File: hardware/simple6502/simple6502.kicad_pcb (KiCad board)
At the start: 2 copper layers, 100 x 100 mm, 40 parts, among them J1 ~{VP}, J2 CLK SEL, J3 RESET, J4 GND, J5 POWER 5V, J6 AUX 5VDC, J7 FTDI Serial, J8 USB Power, J9 Expansion Port, SW1 RESET, SW2 POWER, T1 DS1813, U1 W65C02SxP, U2 RAM 62256, U3 ROM 28C256, U4 74LS30, U5 74HCT00, U6 74HC138, U7 MC68B50, X1 ACO-1MHz

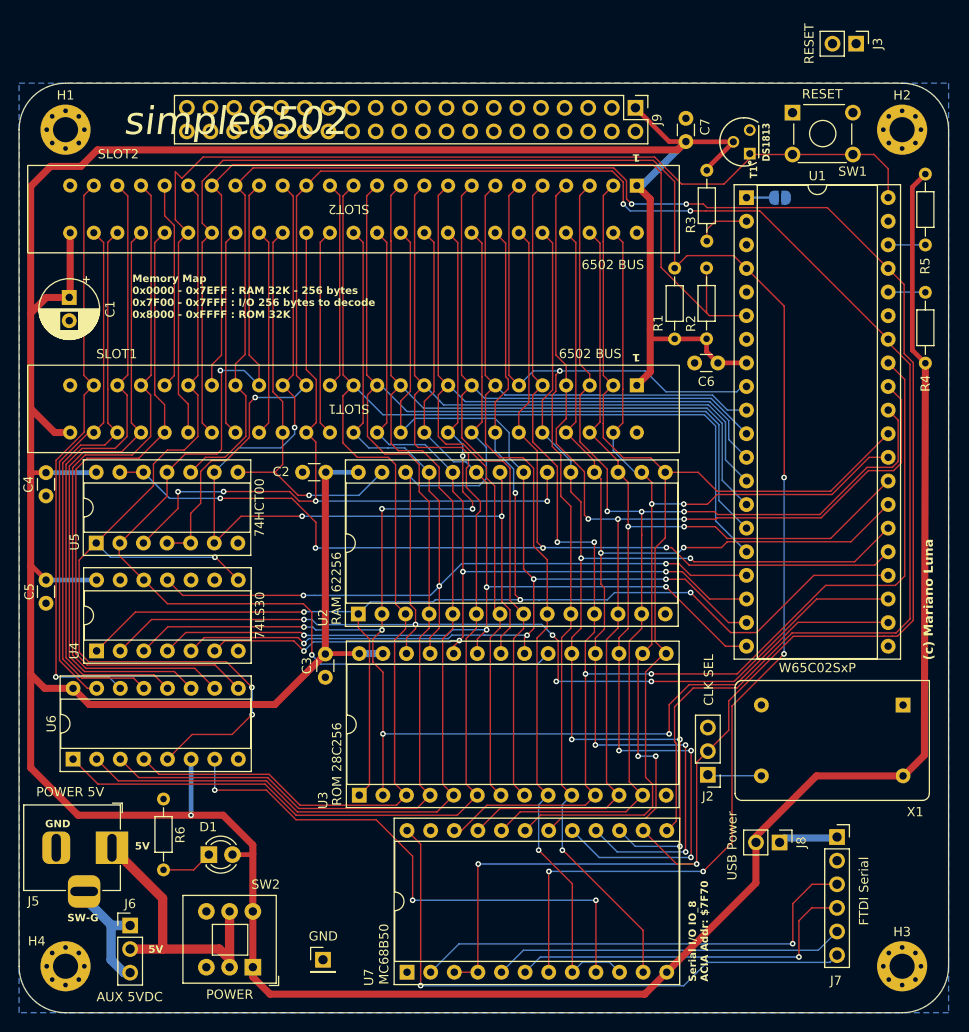
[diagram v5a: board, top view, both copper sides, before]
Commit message: port wired, new slot pinout
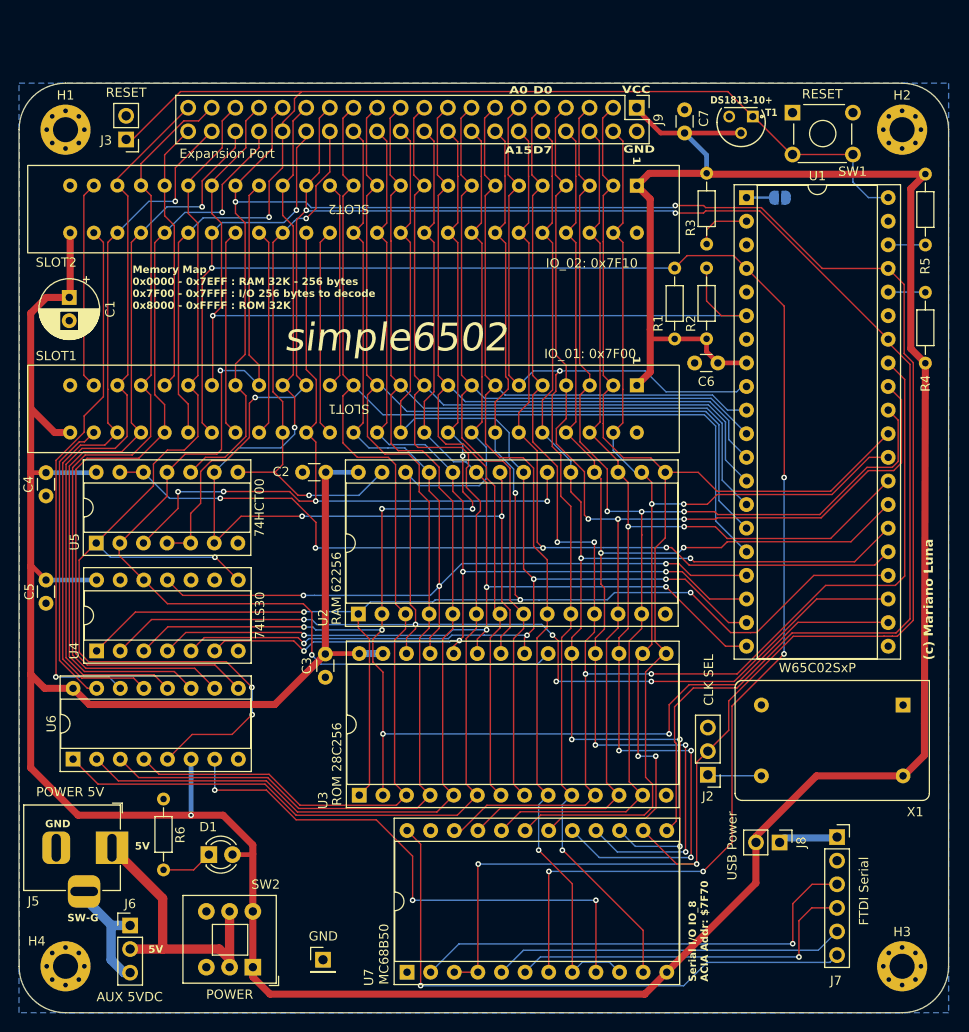
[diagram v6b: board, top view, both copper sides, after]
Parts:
- SLOT1: value 6502 BUS -> IO_01: 0x7F00
- SLOT2: value 6502 BUS -> IO_02: 0x7F10
- T1: value DS1813 -> DS1813-10+
- moved J3 79.2 mm to (61.5, 56.0), turned to 180 degrees
- moved T1 0.96 mm to (126.4, 54.9), turned to 180 degrees
- moved C7 0.93 mm to (121.6, 55.4)
- moved R3 0.32 mm to (124.0, 67.3)
- moved J9 0.14 mm to (116.5, 52.6)
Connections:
- net NC33 renamed BUS_33
- net NC34 renamed BUS_34
- J9 pad 10: unconnected-(J9-Pin_10-Pad10) -> D7
- J9 pad 11: unconnected-(J9-Pin_11-Pad11) -> A0
- J9 pad 12: unconnected-(J9-Pin_12-Pad12) -> A15
- J9 pad 13: unconnected-(J9-Pin_13-Pad13) -> A1
- J9 pad 14: unconnected-(J9-Pin_14-Pad14) -> A14
- J9 pad 15: unconnected-(J9-Pin_15-Pad15) -> A2
- J9 pad 16: unconnected-(J9-Pin_16-Pad16) -> A13
- J9 pad 17: unconnected-(J9-Pin_17-Pad17) -> A3
- J9 pad 18: unconnected-(J9-Pin_18-Pad18) -> A12
- J9 pad 19: unconnected-(J9-Pin_19-Pad19) -> A4
- J9 pad 20: unconnected-(J9-Pin_20-Pad20) -> A11
- J9 pad 21: unconnected-(J9-Pin_21-Pad21) -> A5
- J9 pad 22: unconnected-(J9-Pin_22-Pad22) -> A10
- J9 pad 23: unconnected-(J9-Pin_23-Pad23) -> A6
- J9 pad 24: unconnected-(J9-Pin_24-Pad24) -> A9
- J9 pad 25: unconnected-(J9-Pin_25-Pad25) -> A7
- J9 pad 26: unconnected-(J9-Pin_26-Pad26) -> A8
- J9 pad 27: unconnected-(J9-Pin_27-Pad27) -> R~{W}
- J9 pad 28: unconnected-(J9-Pin_28-Pad28) -> ~{WR}
- J9 pad 29: unconnected-(J9-Pin_29-Pad29) -> ~{RD}
- J9 pad 3: unconnected-(J9-Pin_3-Pad3) -> D3
- J9 pad 30: unconnected-(J9-Pin_30-Pad30) -> ~{IRQ}
- J9 pad 31: unconnected-(J9-Pin_31-Pad31) -> CLK
- J9 pad 32: unconnected-(J9-Pin_32-Pad32) -> ~{RESET}
- J9 pad 33: unconnected-(J9-Pin_33-Pad33) -> ~{NMI}
- J9 pad 34: unconnected-(J9-Pin_34-Pad34) -> ~{IO_07}
- J9 pad 35: unconnected-(J9-Pin_35-Pad35) -> ~{IO_CS}
- J9 pad 36: unconnected-(J9-Pin_36-Pad36) -> ~{IO_05}
- J9 pad 37: unconnected-(J9-Pin_37-Pad37) -> ~{IO_06}
- J9 pad 38: unconnected-(J9-Pin_38-Pad38) -> ~{IO_03}
- J9 pad 39: unconnected-(J9-Pin_39-Pad39) -> ~{IO_04}
- J9 pad 4: unconnected-(J9-Pin_4-Pad4) -> D4
- J9 pad 40: unconnected-(J9-Pin_40-Pad40) -> BUS_21
- J9 pad 5: unconnected-(J9-Pin_5-Pad5) -> D2
- J9 pad 6: unconnected-(J9-Pin_6-Pad6) -> D5
- J9 pad 7: unconnected-(J9-Pin_7-Pad7) -> D1
- J9 pad 8: unconnected-(J9-Pin_8-Pad8) -> D6
- J9 pad 9: unconnected-(J9-Pin_9-Pad9) -> D0
- SLOT1 pad 21: ~{IO_NC} -> BUS_21
- SLOT1 pad 24: ~{IO_02} -> BUS_24
- SLOT2 pad 21: ~{IO_NC} -> BUS_21
- SLOT2 pad 24: ~{IO_02} -> BUS_24
- SLOT2 pad 27: ~{IO_01} -> ~{IO_02}
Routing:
- net VCC: track 491.4 -> 431.5 mm
- net BUS_21: track 0.00 -> 29.2 mm
- net ~{RESET}: track 114.1 -> 137.3 mm, vias 0 -> 1
- net BUS_24: track 0.00 -> 22.4 mm
- net ~{IO_01}: track 54.0 -> 31.6 mm
- net ~{IO_NC}: track 22.4 -> 0.00 mm
- net ~{IO_07}: track 72.4 -> 89.9 mm, vias 0 -> 1
- net ~{IO_05}: track 66.6 -> 83.9 mm, vias 0 -> 1
- net ~{IO_03}: track 60.7 -> 77.5 mm, vias 0 -> 1
- net ~{WR}: track 44.5 -> 58.1 mm, vias 1 -> 2
- net ~{IO_06}: track 75.0 -> 87.5 mm
- net A15: track 125.0 -> 136.8 mm
- net D5: track 123.1 -> 134.8 mm
- net D6: track 123.0 -> 134.8 mm
- net D7: track 122.6 -> 134.4 mm
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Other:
- board text added: "A0"
- board text added: "A15"
- board text added: "D0"
- board text added: "D7"
- board text added: "VCC"

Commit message: minor route changes
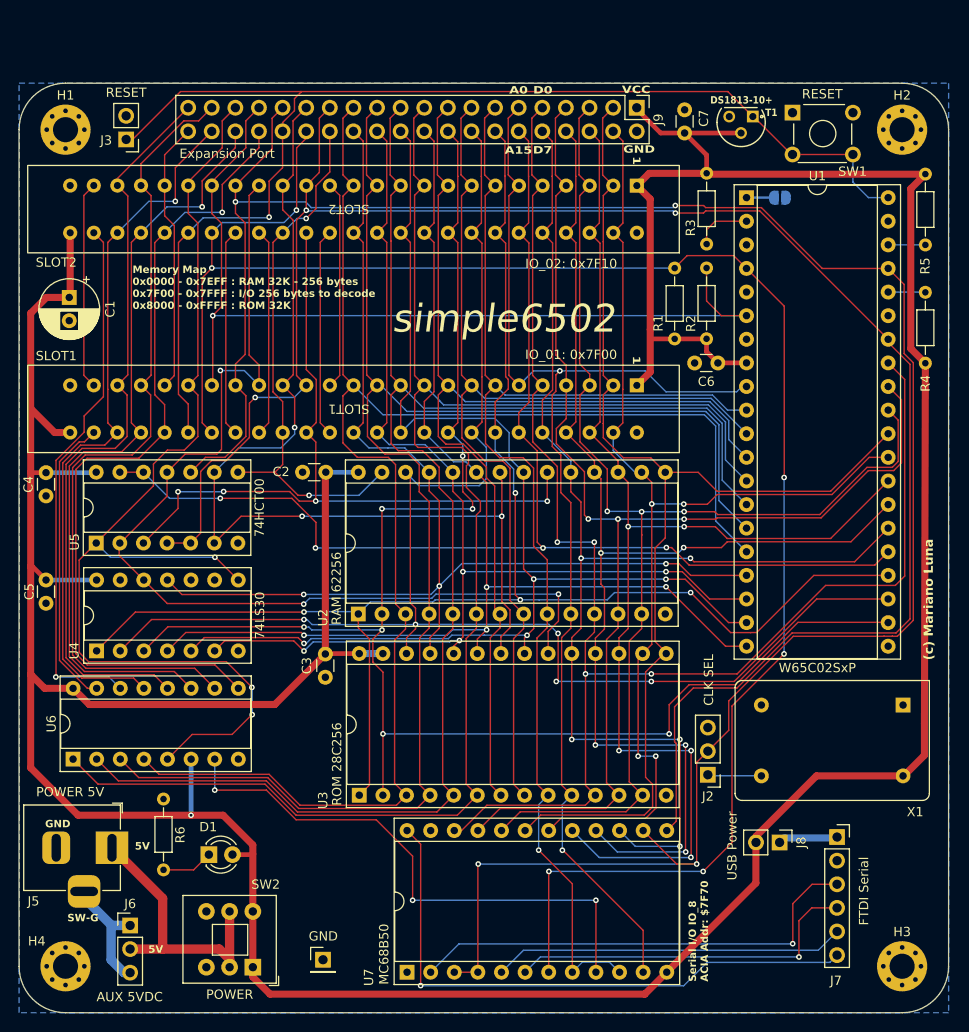
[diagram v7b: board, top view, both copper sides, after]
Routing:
- net ~{ROM_CS}: track 107.9 -> 110.4 mm, vias 2 -> 3
- net VCC: track 431.5 -> 430.8 mm

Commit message: renumer components based on PCB placement
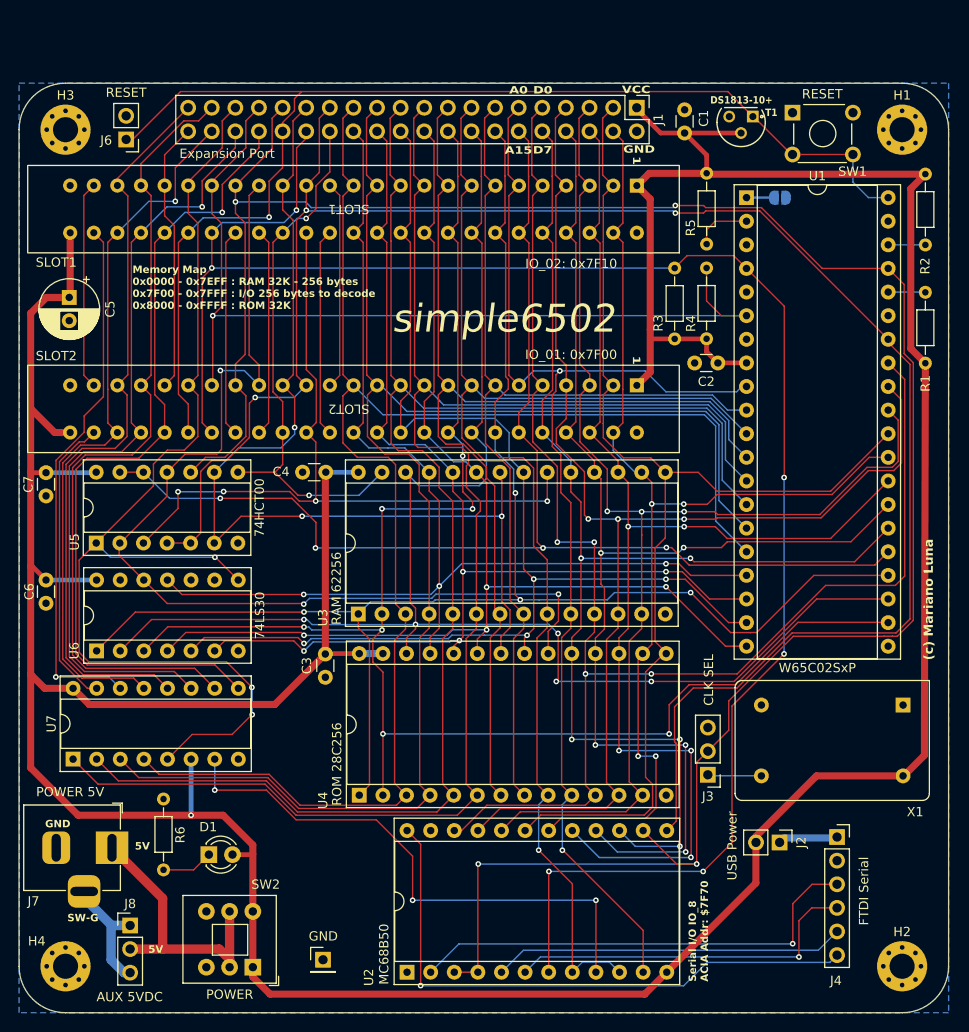
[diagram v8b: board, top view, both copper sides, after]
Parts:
- renumbered C7 to C1, C6 to C2, C2 to C4, C1 to C5, C5 to C6, C4 to C7, H2 to H1, H3 to H2, H1 to H3, J9 to J1, J8 to J2, J2 to J3, J7 to J4, J4 to J5, J3 to J6, J5 to J7, J6 to J8, J1 to J9, R4 to R1, R5 to R2, R1 to R3, R2 to R4, R3 to R5, SLOT2 to SLOT1, SLOT1 to SLOT2, U7 to U2, U2 to U3, U3 to U4, U4 to U6, U6 to U7
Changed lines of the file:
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@@
     (property "ki_keywords" "demux")
     (attr through_hole)
-    (fp_text reference "U6" (at 3.81 -2.33 90) (layer "F.SilkS")
+    (fp_text reference "U7" (at 3.81 -2.33 90) (layer "F.SilkS")
         (effects (font (size 1 1) (thickness 0.15)))
     )
@@
     (property "ki_keywords" "cap capacitor")
     (attr through_hole)
-    (fp_text reference "C1" (at 1.25 -4.4 90) (layer "F.SilkS")
+    (fp_text reference "C5" (at 1.25 -4.4 90) (layer "F.SilkS")
         (effects (font (size 1 1) (thickness 0.15)))
     )
@@
     (property "ki_keywords" "R res resistor")
     (attr through_hole)
-    (fp_text reference "R4" (at 9.79 -0.01 90) (layer "F.SilkS")
+    (fp_text reference "R1" (at 9.79 -0.01 90) (layer "F.SilkS")
         (effects (font (size 1 1) (thickness 0.15)))
     )
@@
     (property "ki_keywords" "R res resistor")
     (attr through_hole)
-    (fp_text reference "R5" (at -2.26 -0.02 90) (layer "F.SilkS")
+    (fp_text reference "R2" (at -2.26 -0.02 90) (layer "F.SilkS")
         (effects (font (size 1 1) (thickness 0.15)))
     )
@@
     (property "ki_keywords" "connector")
     (attr through_hole)
-    (fp_text reference "SLOT2" (at 0.508 0 180 unlocked) (layer "F.SilkS")
+    (fp_text reference "SLOT1" (at 0.508 0 180 unlocked) (layer "F.SilkS")
         (effects (font (size 1 1) (thickness 0.15)))
     )
@@
     (property "ki_keywords" "cap capacitor")
     (attr through_hole)
-    (fp_text reference "C4" (at 1.25 1.9 90) (layer "F.SilkS")
+    (fp_text reference "C7" (at 1.25 1.9 90) (layer "F.SilkS")
         (effects (font (size 1 1) (thickness 0.15)))
     )
@@
     (property "ki_keywords" "cap capacitor")
     (attr through_hole)
-    (fp_text reference "C5" (at 1.25 1.8 90) (layer "F.SilkS")
+    (fp_text reference "C6" (at 1.25 1.8 90) (layer "F.SilkS")
         (effects (font (size 1 1) (thickness 0.15)))
     )
@@
     (property "ki_keywords" "connector")
     (attr through_hole)
-    (fp_text reference "SLOT1" (at 0.508 0 180 unlocked) (layer "F.SilkS")
+    (fp_text reference "SLOT2" (at 0.508 0 180 unlocked) (layer "F.SilkS")
         (effects (font (size 1 1) (thickness 0.15)))
     )
@@
     (property "ki_keywords" "R res resistor")
     (attr through_hole)
-    (fp_text reference "R2" (at 5.98 1.68 90) (layer "F.SilkS")
+    (fp_text reference "R4" (at 5.98 1.68 90) (layer "F.SilkS")
         (effects (font (size 1 1) (thickness 0.15)))
     )
@@
     (property "ki_keywords" "cap capacitor")
     (attr through_hole)
-    (fp_text reference "C7" (at 1.58 2.06 90) (layer "F.SilkS")
+    (fp_text reference "C1" (at 1.58 2.06 90) (layer "F.SilkS")
         (effects (font (size 1 1) (thickness 0.15)))
     )
@@
     (property "ki_keywords" "connector")
     (attr through_hole)
-    (fp_text reference "J4" (at 0 -2.33) (layer "F.SilkS") hide
+    (fp_text reference "J5" (at 0 -2.33) (layer "F.SilkS") hide
         (effects (font (size 1 1) (thickness 0.15)))
     )
@@
     (property "ki_keywords" "connector")
     (attr through_hole)
-    (fp_text reference "J6" (at 0 -2.33) (layer "F.SilkS")
+    (fp_text reference "J8" (at 0 -2.33) (layer "F.SilkS")
         (effects (font (size 1 1) (thickness 0.15)))
     )
@@
     (property "ki_keywords" "mounting hole")
     (attr exclude_from_pos_files)
-    (fp_text reference "H1" (at 0 -3.7) (layer "F.SilkS")
+    (fp_text reference "H3" (at 0 -3.7) (layer "F.SilkS")
         (effects (font (size 1 1) (thickness 0.15)))
     )
@@
     (property "ki_keywords" "Parallel EEPROM 256Kb")
     (attr through_hole)
-    (fp_text reference "U3" (at -0.55 -3.9 90) (layer "F.SilkS")
+    (fp_text reference "U4" (at -0.55 -3.9 90) (layer "F.SilkS")
         (effects (font (size 1 1) (thickness 0.15)))
     )
@@
     (property "ki_keywords" "connector")
     (attr through_hole)
-    (fp_text reference "J2" (at 0 -2.33 180) (layer "F.SilkS")
+    (fp_text reference "J3" (at 0 -2.33 180) (layer "F.SilkS")
         (effects (font (size 1 1) (thickness 0.15)))
     )
@@
     (property "ki_keywords" "DC power barrel jack connector")
     (attr through_hole)
-    (fp_text reference "J5" (at -8.45 5.75) (layer "F.SilkS")
+    (fp_text reference "J7" (at -8.45 5.75) (layer "F.SilkS")
         (effects (font (size 1 1) (thickness 0.15)))
     )
@@
     (property "ki_keywords" "connector")
     (attr through_hole)
-    (fp_text reference "J3" (at 2.15 -0.1) (layer "F.SilkS")
+    (fp_text reference "J6" (at 2.15 -0.1) (layer "F.SilkS")
         (effects (font (size 1 1) (thickness 0.15)))
     )
@@
     (property "ki_keywords" "ACIA")
     (attr through_hole)
-    (fp_text reference "U7" (at -0.55 -4.11 90) (layer "F.SilkS")
+    (fp_text reference "U2" (at -0.55 -4.11 90) (layer "F.SilkS")
         (effects (font (size 1 1) (thickness 0.15)))
     )
@@
     (property "ki_keywords" "R res resistor")
     (attr through_hole)
-    (fp_text reference "R3" (at 1.75 -1.72 90) (layer "F.SilkS")
+    (fp_text reference "R5" (at 1.75 -1.72 90) (layer "F.SilkS")
         (effects (font (size 1 1) (thickness 0.15)))
     )
@@
     (property "ki_keywords" "connector")
     (attr through_hole)
-    (fp_text reference "J8" (at 0 -2.33 90) (layer "F.SilkS")
+    (fp_text reference "J2" (at 0 -2.33 90) (layer "F.SilkS")
         (effects (font (size 1 1) (thickness 0.15)))
     )
@@
     (property "ki_keywords" "connector")
     (attr through_hole)
-    (fp_text reference "J9" (at 1.27 -2.33 -90) (layer "F.SilkS")
+    (fp_text reference "J1" (at 1.27 -2.33 -90) (layer "F.SilkS")
         (effects (font (size 1 1) (thickness 0.15)))
     )
@@
     (property "ki_keywords" "connector")
     (attr through_hole)
-    (fp_text reference "J7" (at -0.12 15.45) (layer "F.SilkS")
+    (fp_text reference "J4" (at -0.12 15.45) (layer "F.SilkS")
         (effects (font (size 1 1) (thickness 0.15)))
     )
@@
     (property "ki_keywords" "R res resistor")
     (attr through_hole)
-    (fp_text reference "R1" (at 5.93 1.76 90) (layer "F.SilkS")
+    (fp_text reference "R3" (at 5.93 1.76 90) (layer "F.SilkS")
         (effects (font (size 1 1) (thickness 0.15)))
     )
@@
     (property "ki_keywords" "TTL Nand8")
     (attr through_hole)
-    (fp_text reference "U4" (at 0.02 -2.4 90) (layer "F.SilkS")
+    (fp_text reference "U6" (at 0.02 -2.4 90) (layer "F.SilkS")
         (effects (font (size 1 1) (thickness 0.15)))
     )
@@
     (property "ki_keywords" "RAM SRAM CMOS MEMORY")
     (attr through_hole)
-    (fp_text reference "U2" (at -0.4 -3.8 90) (layer "F.SilkS")
+    (fp_text reference "U3" (at -0.4 -3.8 90) (layer "F.SilkS")
         (effects (font (size 1 1) (thickness 0.15)))
     )
@@
     (property "ki_keywords" "mounting hole")
     (attr exclude_from_pos_files)
-    (fp_text reference "H3" (at 0 -3.7) (layer "F.SilkS")
+    (fp_text reference "H2" (at 0 -3.7) (layer "F.SilkS")
         (effects (font (size 1 1) (thickness 0.15)))
     )
@@
     (property "ki_keywords" "cap capacitor")
     (attr through_hole)
-    (fp_text reference "C2" (at 4.81 0.05) (layer "F.SilkS")
+    (fp_text reference "C4" (at 4.81 0.05) (layer "F.SilkS")
         (effects (font (size 1 1) (thickness 0.15)))
     )
@@
     (property "ki_keywords" "cap capacitor")
     (attr through_hole)
-    (fp_text reference "C6" (at 1.25 -2) (layer "F.SilkS")
+    (fp_text reference "C2" (at 1.25 -2) (layer "F.SilkS")
         (effects (font (size 1 1) (thickness 0.15)))
     )
@@
     (property "ki_keywords" "mounting hole")
     (attr exclude_from_pos_files)
-    (fp_text reference "H2" (at 0 -3.7) (layer "F.SilkS")
+    (fp_text reference "H1" (at 0 -3.7) (layer "F.SilkS")
         (effects (font (size 1 1) (thickness 0.15)))
     )
@@
     (property "ki_keywords" "connector")
     (attr exclude_from_pos_files)
-    (fp_text reference "J1" (at 0 1.8) (layer "B.SilkS")
+    (fp_text reference "J9" (at 0 1.8) (layer "B.SilkS")
         (effects (font (size 1 1) (thickness 0.15)) (justify mirror))
     )
